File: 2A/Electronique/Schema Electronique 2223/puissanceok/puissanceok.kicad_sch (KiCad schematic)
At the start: 33 parts, among them J10 Conn_01x05, J11 Conn_Phidget_PS_Stepper_1, J12 Conn_01x02, J13 Conn_Phidget_PS_Stepper_2, J14 Conn_Phidget_PS_Stepper_3, J15 Conn_Phidget_PS_Stepper_4, J5 Conn_GND, J6 Conn_GPIO_unused, J7 Conn_3.3V, J9 Conn_01x05

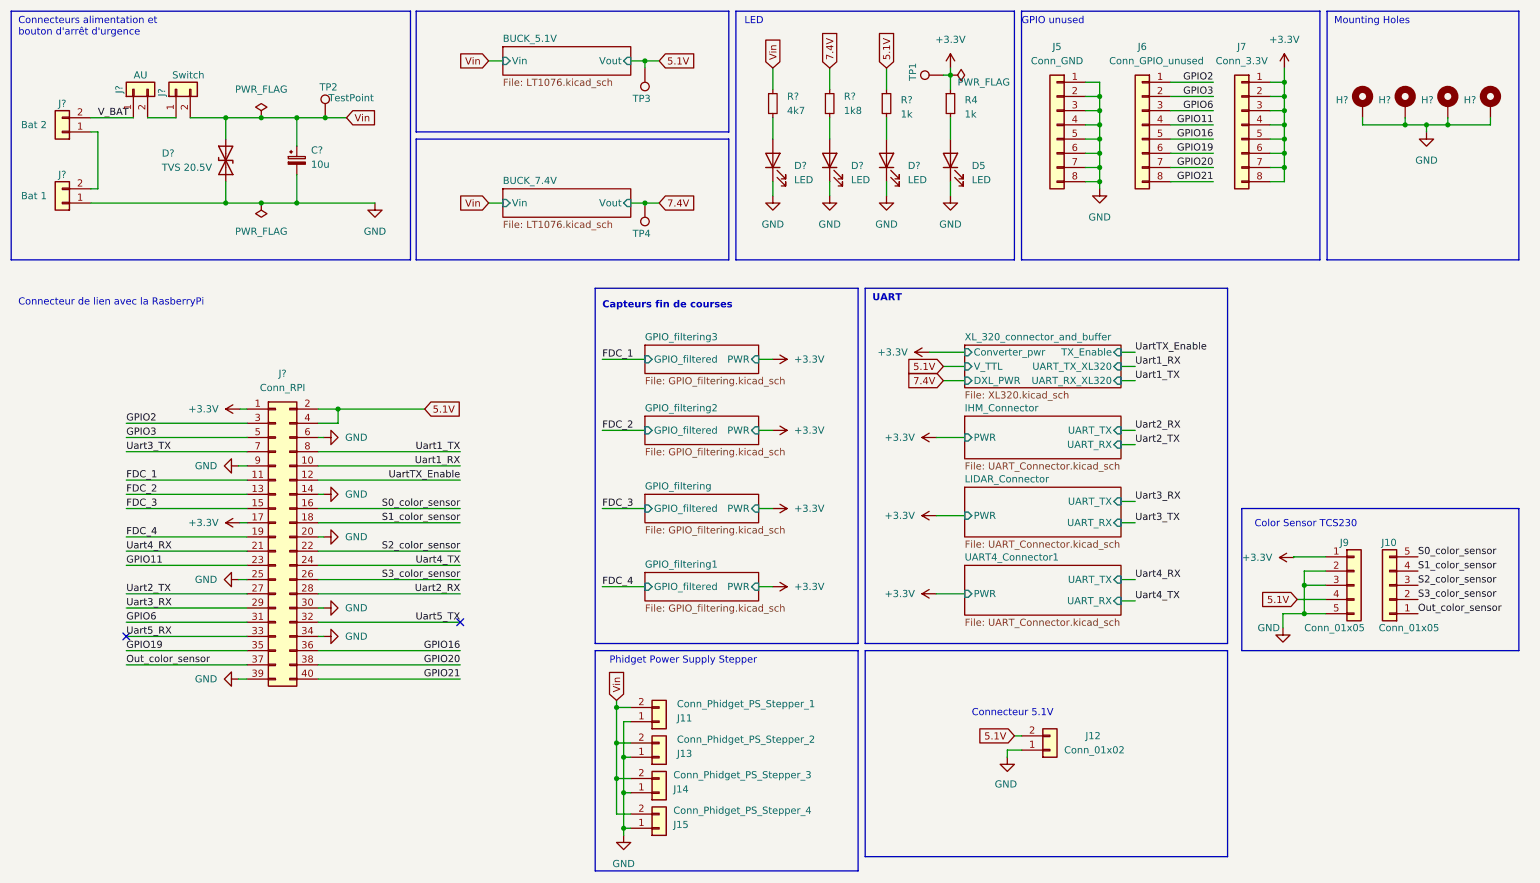
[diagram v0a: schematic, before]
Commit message: pcb place components and add power/gnd planes
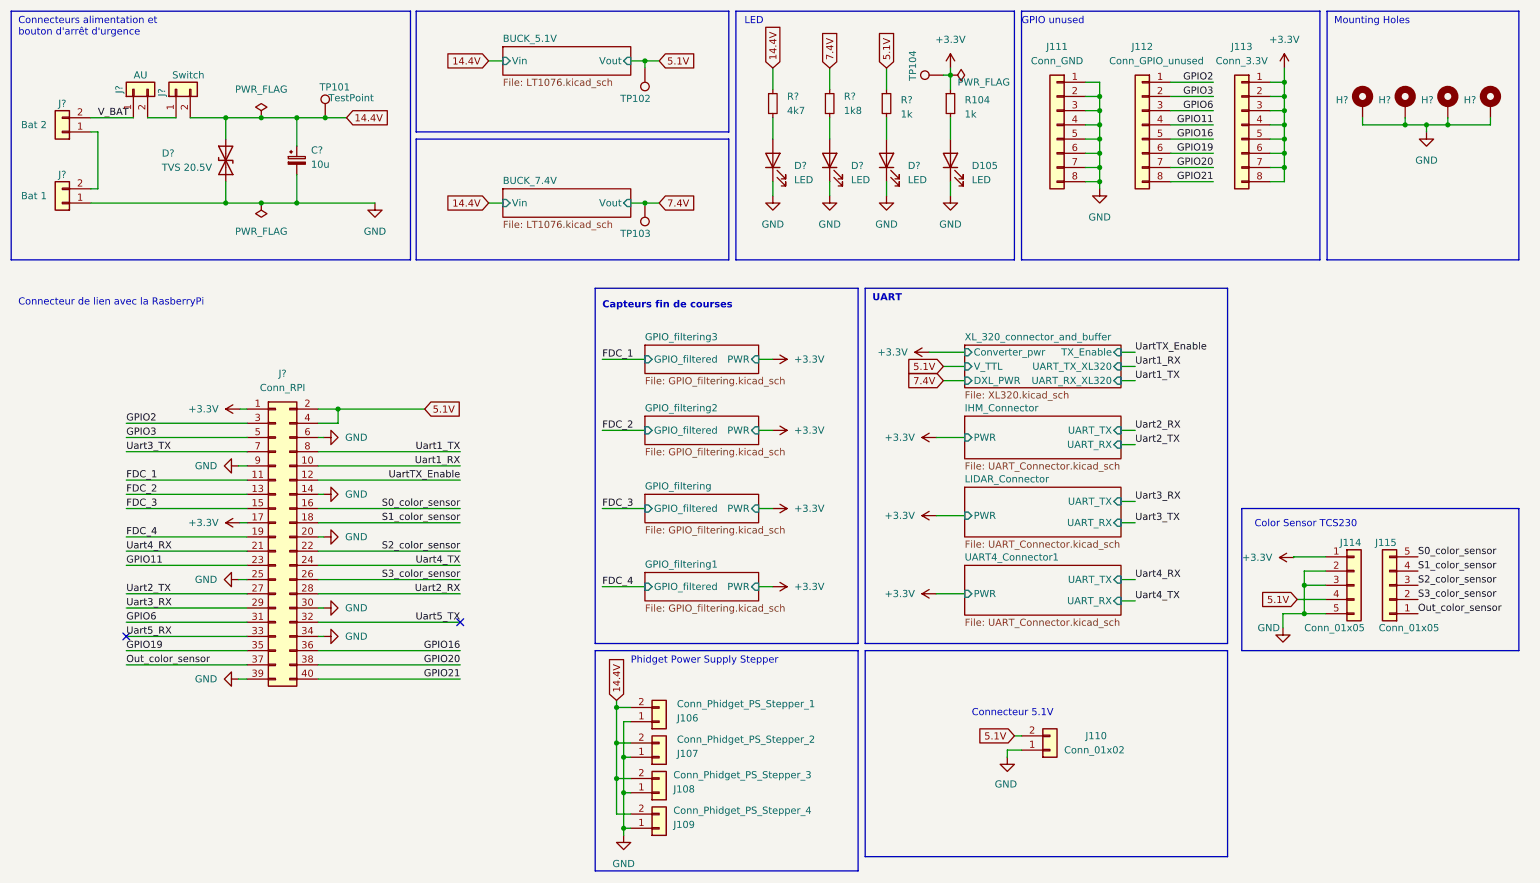
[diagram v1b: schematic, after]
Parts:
- renumbered D5 to D105, J11 to J106, J13 to J107, J14 to J108, J15 to J109, J12 to J110, J5 to J111, J6 to J112, J7 to J113, J9 to J114, J10 to J115, R4 to R104, TP2 to TP101, TP3 to TP102, TP4 to TP103, TP1 to TP104
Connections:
- net Vin renamed 14.4V
